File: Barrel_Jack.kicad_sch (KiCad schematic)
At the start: 6 parts, among them J6 Barrel_Jack, Q2 MOSFET-NCHANNELSMD, U12 PCF8574ATS

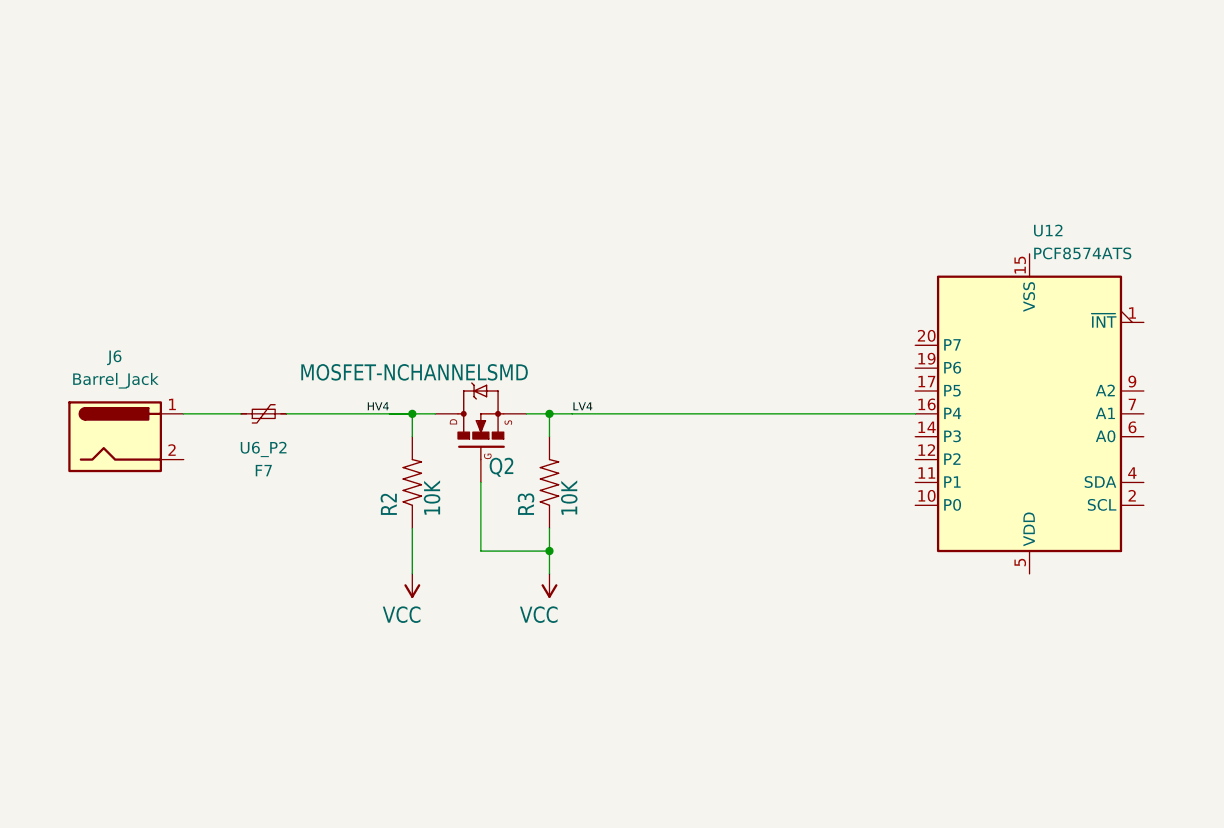
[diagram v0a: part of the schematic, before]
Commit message: added layout from online made room for full 41f switch
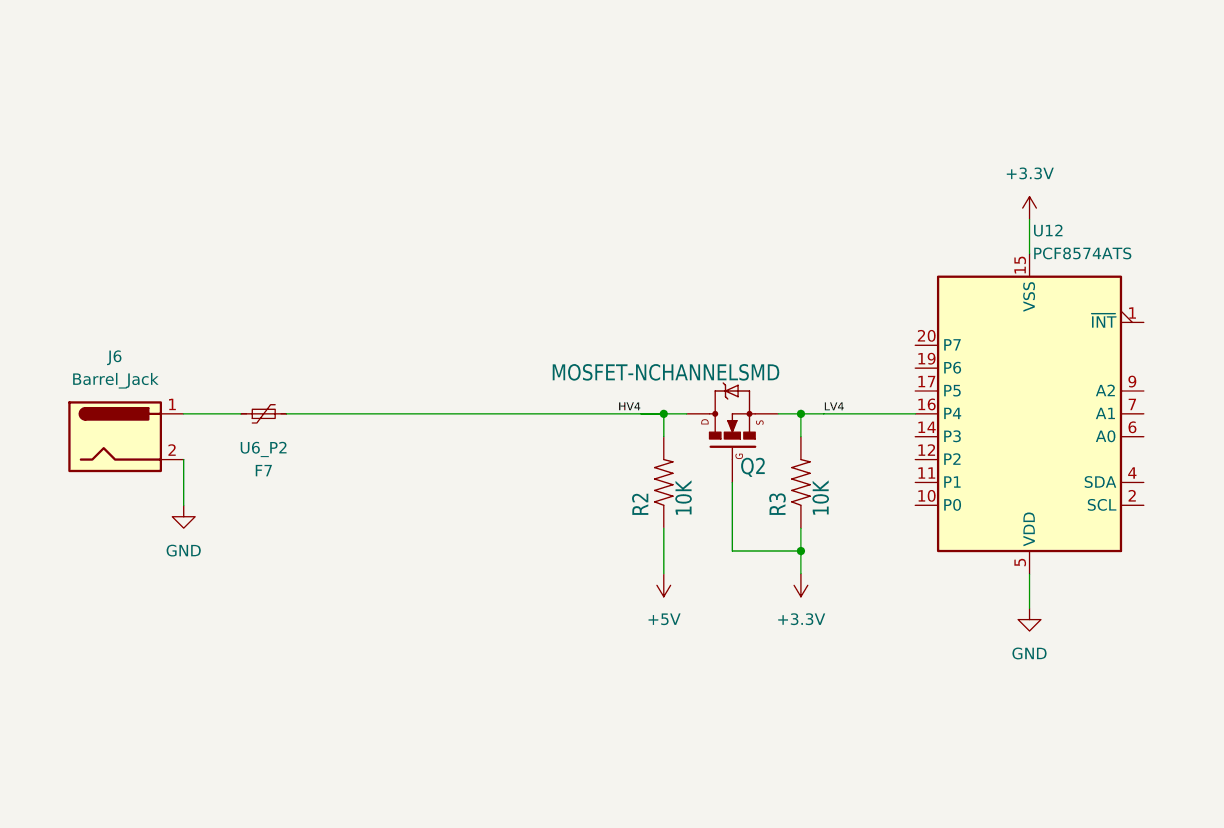
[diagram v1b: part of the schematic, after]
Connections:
- net GND: now reaches J6.2
- net GND: now also U12.5 (VDD)
- net +3.3V: now reaches U12.15 (VSS)
- net +3.3V: now also Q2.1 (G), R3.1
- removed net VCC: Q2.1 (G), R2.1, R3.1
- new net +5V: R2.1
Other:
- moved on the sheet: Q2, R2, R3

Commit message: main sheet barrel connector
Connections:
- net PCA0_SDA_0: now reaches U12.2 (SCL)
- net PCA0_SCL_0: now reaches U12.4 (SDA)
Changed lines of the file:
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@@
     (effects (font (size 0.889 0.889)) (justify left bottom))
+  )
+  (hierarchical_label "PCA0_SDA_0" (shape bidirectional) (at 226.06 93.98 0) (fields_autoplaced)
+    (effects (font (size 1.27 1.27)) (justify left))
+  )
+  (hierarchical_label "PCA0_SDA_8-15" (shape input) (at 251.46 76.2 0) (fields_autoplaced)
+    (effects (font (size 1.27 1.27)) (justify left))
+  )
+  (hierarchical_label "PCA0_SCL_0" (shape input) (at 226.06 91.44 0) (fields_autoplaced)
+    (effects (font (size 1.27 1.27)) (justify left))
   )
   (symbol (lib_id "Device:Polyfuse_Small") (at 128.27 83.82 90) (unit 1)

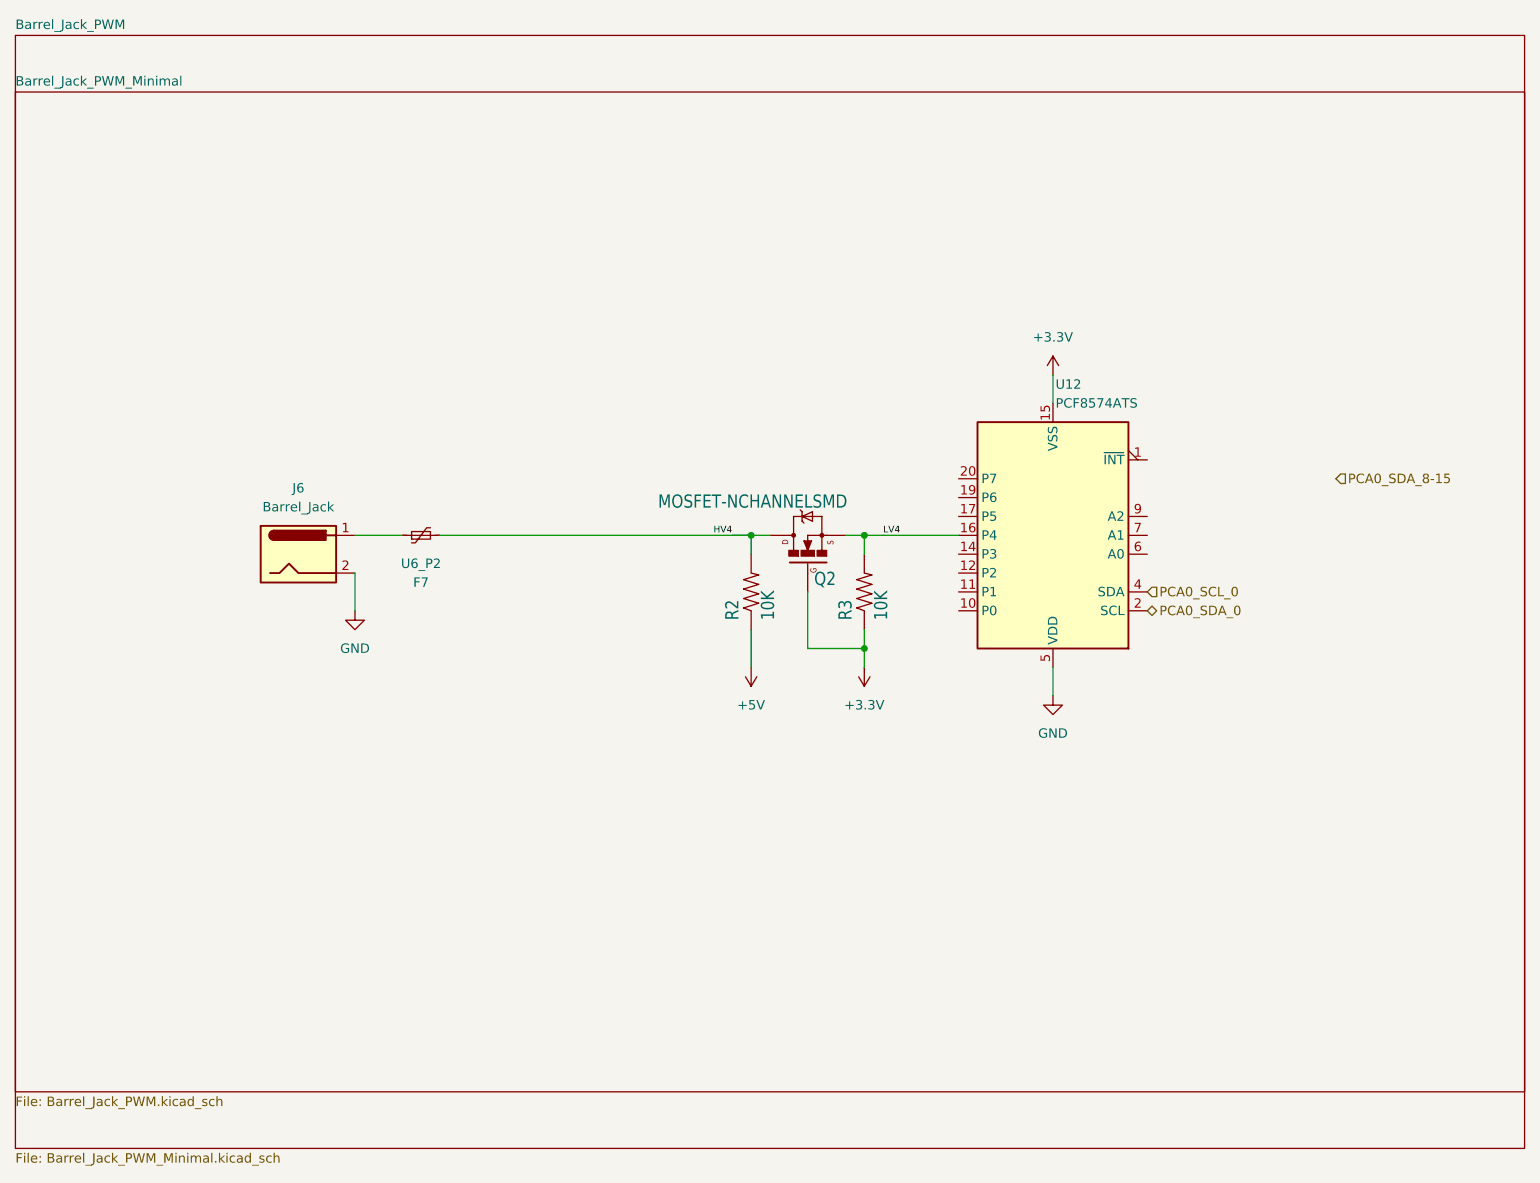
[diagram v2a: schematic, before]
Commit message: PCB can be built, naming issues
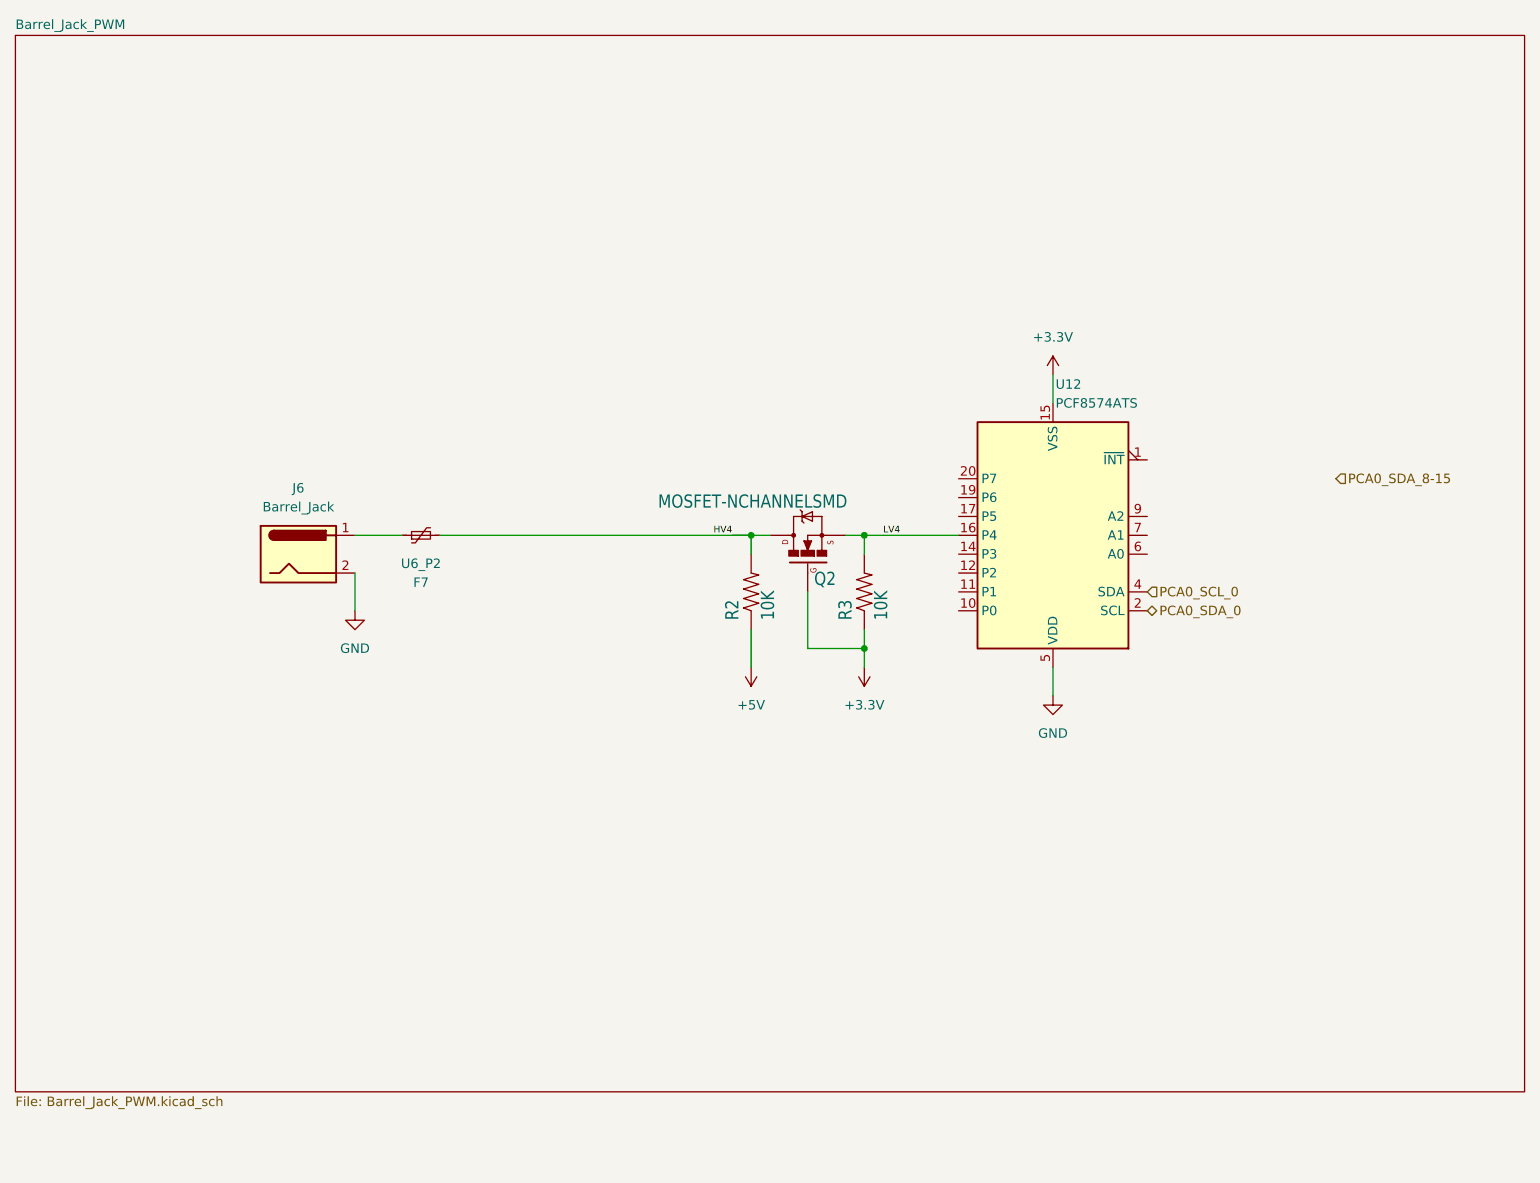
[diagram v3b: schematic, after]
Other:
- removed sheet Barrel_Jack_PWM_Minimal
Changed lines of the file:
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@@
-    )
-  )
-  (sheet (at 73.66 24.13) (size 203.2 142.24) (fields_autoplaced)
-    (stroke (width 0.1524) (type solid))
-    (fill (color 0 0 0 0.0000))
-    (property "Sheetname" "Barrel_Jack_PWM_Minimal" (at 73.66 23.4184 0)
-      (effects (font (size 1.27 1.27)) (justify left bottom))
-    )
-    (property "Sheetfile" "Barrel_Jack_PWM_Minimal.kicad_sch" (at 73.66 166.9546 0)
-      (effects (font (size 1.27 1.27)) (justify left top))
-    )
-    (instances
-      (project "esp"
-        (path "/dab6683c-420f-459a-bf9c-0c28b4b081e3/d534b787-d3bc-419e-b481-23d8b9503201" (page "7"))
-      )
     )
   )

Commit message: slimmed down and spread out pcb
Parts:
- removed F7: U6_P2, symbol Device:Polyfuse_Small
- removed J6: Barrel_Jack, symbol Connector:Barrel_Jack
- removed Q2: MOSFET-NCHANNELSMD, Logic_Level_Bidirectional:SOT23-3, symbol Logic_Level_Bidirectional-eagle-import:MOSFET-NCHANNELSMD
- removed R2, R3: 10K, Logic_Level_Bidirectional:0603-RES, symbol Logic_Level_Bidirectional-eagle-import:RESISTOR0603-RES
- removed U12: PCF8574ATS, Package_SO:SSOP-20_4.4x6.5mm_P0.65mm, symbol Interface_Expansion:PCF8574ATS
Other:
- removed sheet Barrel_Jack_PWM
